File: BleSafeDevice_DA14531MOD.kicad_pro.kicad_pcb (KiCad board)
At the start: 2 copper layers, 43.5 x 33.5 mm, 21 parts, among them J1 Conn_01x04, J2 EXT_PWR, SW1 1825910-6, U4 DA14531MOD-00F01002

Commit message: Sync PCB with schematic cleanup
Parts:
- removed D2: BAT54, myparts:SOT95P240X120-3N
- removed S1: MSK12C02, Button_Switch_SMD:SW_SPDT_PCM12
- C1: value 47uF 6.3V -> 100uF 6.3V
- D1: value LED_ARGB -> LRTBR48G-P9Q7-1; footprint LED_SMD:LED_RGB_Wuerth-PLCC4_3.2x2.8mm_150141M173100 -> SafeGuardPing_Local:LED_RGB_amsOSRAM_LRTBR48G
- J2: value EXT_PWR -> CURRENT_MEAS_PADS
- JP1: value JP_EXT_TO_VCC -> CURRENT_MEAS_JUMPER
- SW1: value 1825910-6 -> PTS526SK15SMTR2 LFS; footprint 1825910-6:SW4_1825910-B_TEC -> SafeGuardPing_Local:SW_Push_1P1T_NO_CK_PTS526SK15SMTR2_LFS
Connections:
- J2 pad 1: Net-(J2-Pin_1) -> VBAT
- JP1 pad 1: Net-(J2-Pin_1) -> VBAT

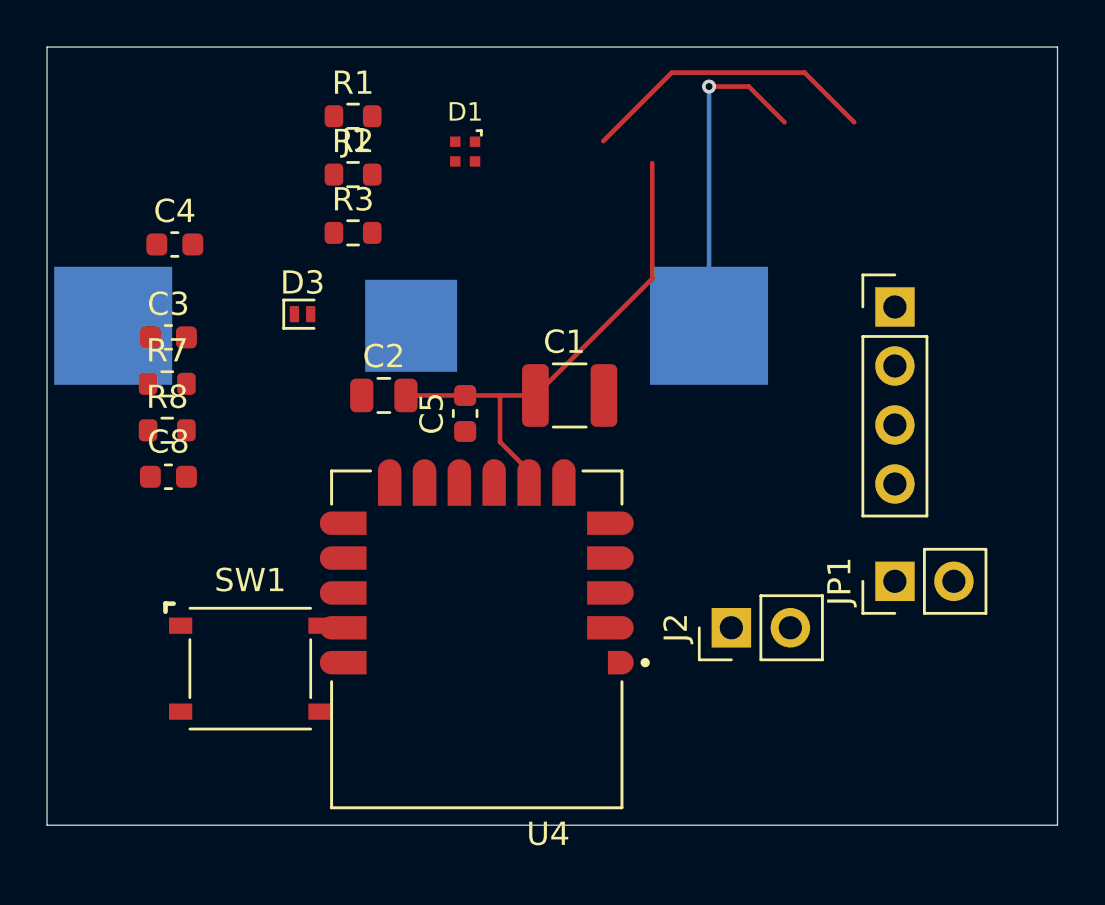
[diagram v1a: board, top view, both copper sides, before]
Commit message: Clean PCB placement after schematic sync
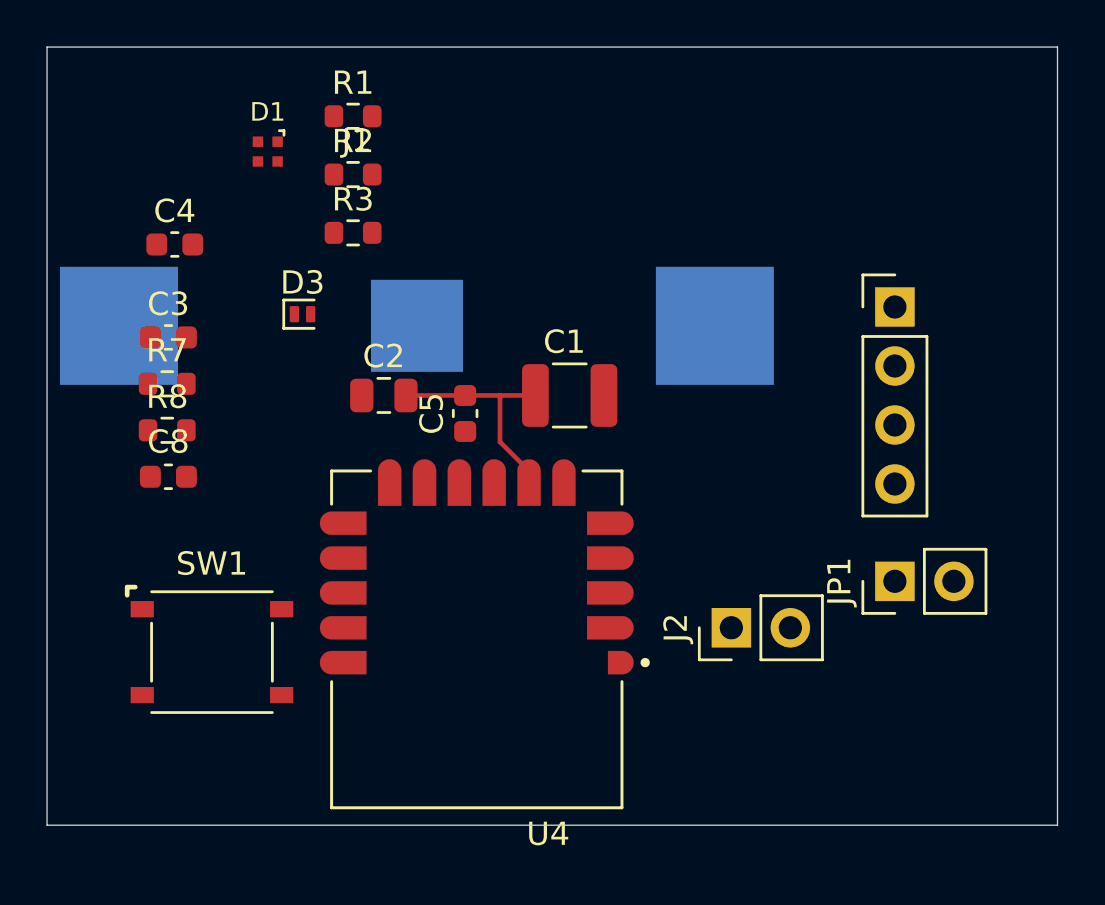
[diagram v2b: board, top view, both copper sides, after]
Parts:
- moved D1 8.50 mm to (108.5, 101.0)
- moved SW1 1.80 mm to (106.1, 122.5)
- moved BT1 0.25 mm to (114.9, 108.5)
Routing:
- net VBAT: track 14.2 -> 0.00 mm, vias 1 -> 0
- net Net-(D2-Pad1): track 12.9 -> 0.00 mm
- net VCC: track 21.9 -> 9.84 mm
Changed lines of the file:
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@@
 	(net 6 "Net-(D1-GK)")
 	(net 7 "Net-(D1-RK)")
-	(net 8 "Net-(D2-Pad1)")
-	(net 9 "Net-(D3-K)")
-	(net 10 "/SWCLK")
-	(net 11 "/SWDIO")
-	(net 12 "LED_R")
-	(net 13 "LED_G")
-	(net 14 "LED_B")
-	(net 15 "unconnected-(U4-P0_0{slash}RST-PadJ12)")
-	(net 16 "unconnected-(U4-P0_5-PadJ14)")
-	(net 17 "unconnected-(U4-P0_11-PadJ8)")
+	(net 8 "Net-(D3-K)")
+	(net 9 "/SWCLK")
+	(net 10 "/SWDIO")
+	(net 11 "LED_R")
+	(net 12 "LED_G")
+	(net 13 "LED_B")
+	(net 14 "unconnected-(U4-P0_0{slash}RST-PadJ12)")
+	(net 15 "unconnected-(U4-P0_5-PadJ14)")
+	(net 16 "unconnected-(U4-P0_11-PadJ8)")
 	(footprint "Diode_SMD:D_SOD-882"
 		(layer "F.Cu")
@@
 			(layers "F.Cu" "F.Mask")
 			(roundrect_rratio 0.125)
-			(net 9 "Net-(D3-K)")
+			(net 8 "Net-(D3-K)")
 			(pinfunction "K")
 			(pintype "passive")
@@
 	(footprint "SafeGuardPing_Local:LED_RGB_amsOSRAM_LRTBR48G"
 		(layer "F.Cu")
-		(at 117 101)
+		(at 108.5 101)
 		(descr "ams OSRAM LRTB R48G Multi CHIPLED, 1.0 mm x 1.0 mm, common anode; recommended land pattern from OSRAM Data Sheet Version 1.8, 2018-05-14, pages 20-21")
 		(tags "LED RGB common anode LRTB R48G LRTBR48G")
@@
 			(layers "F.Cu" "F.Mask" "F.Paste")
 			(roundrect_rratio 0.25)
-			(net 9 "Net-(D3-K)")
+			(net 8 "Net-(D3-K)")
 			(pintype "passive")
 		)
@@
 			(layers "*.Cu" "*.Mask")
 			(remove_unused_layers no)
-			(net 11 "/SWDIO")
+			(net 10 "/SWDIO")
 			(pinfunction "Pin_2")
 			(pintype "passive")
@@
 			(layers "*.Cu" "*.Mask")
 			(remove_unused_layers no)
-			(net 10 "/SWCLK")
+			(net 9 "/SWCLK")
 			(pinfunction "Pin_3")
 			(pintype "passive")
@@
 	(footprint "SafeGuardPing_Local:SW_Push_1P1T_NO_CK_PTS526SK15SMTR2_LFS"
 		(layer "F.Cu")
-		(at 107.75 123.2606)
+		(at 106.1 122.55)
 		(descr "C&K/Littelfuse PTS526SK15SMTR2 LFS, 1.5 mm height, no ground pin; land pattern from C&K PTS526 Series datasheet, Feb 2022, page B-34")
 		(tags "tactile switch PTS526 PTS526SK15SMTR2 LFS")
@@
 			(size 1 0.7)
 			(layers "F.Cu" "F.Mask" "F.Paste")
-			(net 9 "Net-(D3-K)")
+			(net 8 "Net-(D3-K)")
 		)
 		(pad "2" smd rect
@@
 			(size 1 0.7)
 			(layers "F.Cu" "F.Mask" "F.Paste")
-			(net 9 "Net-(D3-K)")
+			(net 8 "Net-(D3-K)")
 		)
 		(pad "3" smd rect
@@
 			(layers "F.Cu" "F.Mask" "F.Paste")
 			(roundrect_rratio 0.25)
-			(net 14 "LED_B")
+			(net 13 "LED_B")
 			(pintype "passive")
 		)
@@
 			(layers "F.Cu" "F.Mask" "F.Paste")
 			(roundrect_rratio 0.25)
-			(net 12 "LED_R")
+			(net 11 "LED_R")
 			(pintype "passive")
 		)
@@
 			(layers "F.Cu" "F.Mask" "F.Paste")
 			(roundrect_rratio 0.25)
-			(net 13 "LED_G")
+			(net 12 "LED_G")
 			(pintype "passive")
 		)
@@
 			(size 0.1 0.1)
 			(layers "F.Cu")
-			(net 14 "LED_B")
+			(net 13 "LED_B")
 			(pinfunction "P0_6")
 			(pintype "bidirectional")
@@
 			(size 0.1 0.1)
 			(layers "F.Cu")
-			(net 17 "unconnected-(U4-P0_11-PadJ8)")
+			(net 16 "unconnected-(U4-P0_11-PadJ8)")
 			(pinfunction "P0_11")
 			(pintype "bidirectional+no_connect")
@@
 			(size 0.1 0.1)
 			(layers "F.Cu")
-			(net 11 "/SWDIO")
+			(net 10 "/SWDIO")
 			(pinfunction "P0_10/SWDIO")
 			(pintype "bidirectional")
@@
 			(size 0.1 0.1)
 			(layers "F.Cu")
-			(net 10 "/SWCLK")
+			(net 9 "/SWCLK")
 			(pinfunction "P0_2/SWCLK")
 			(pintype "bidirectional")
@@
 			(size 0.1 0.1)
 			(layers "F.Cu")
-			(net 15 "unconnected-(U4-P0_0{slash}RST-PadJ12)")
+			(net 14 "unconnected-(U4-P0_0{slash}RST-PadJ12)")
 			(pinfunction "P0_0/RST")
 			(pintype "bidirectional+no_connect")
@@
 			(size 0.1 0.1)
 			(layers "F.Cu")
-			(net 13 "LED_G")
+			(net 12 "LED_G")
 			(pinfunction "P0_7")
 			(pintype "bidirectional")
@@
 			(size 0.1 0.1)
 			(layers "F.Cu")
-			(net 16 "unconnected-(U4-P0_5-PadJ14)")
+			(net 15 "unconnected-(U4-P0_5-PadJ14)")
 			(pinfunction "P0_5")
 			(pintype "bidirectional+no_connect")
@@
 			(size 0.1 0.1)
 			(layers "F.Cu")
-			(net 12 "LED_R")
+			(net 11 "LED_R")
 			(pinfunction "P0_8")
 			(pintype "bidirectional")
@@
 	(footprint "Keystone-3002:BAT_3002"
 		(layer "B.Cu")
-		(at 114.675 108.5 180)
+		(at 114.925 108.5 180)
 		(property "Reference" "BT1"
 			(at -12.4534 10.709 0)
@@
 	)
 	(segment
-		(start 127.5 98.201)
-		(end 129.211 98.201)
-		(width 0.2)
-		(layer "F.Cu")
-		(net 1)
-	)
-	(segment
-		(start 129.211 98.201)
-		(end 130.75 99.74)
-		(width 0.2)
-		(layer "F.Cu")
-		(net 1)
-	)
-	(via
-		(at 127.5 98.201)
-		(size 0.6)
-		(drill 0.3)
-		(layers "F.Cu" "B.Cu")
-		(net 1)
-	)
-	(segment
-		(start 127.5 98.201)
-		(end 127.5 108.5)
-		(width 0.2)
-		(layer "B.Cu")
-		(net 1)
-	)
-	(segment
 		(start 118.5 113.5)
 		(end 119.75 114.75)
@@
 	)
 	(segment
-		(start 125.055 106.47)
-		(end 120.025 111.5)
-		(width 0.2)
-		(layer "F.Cu")
-		(net 3)
-	)
-	(segment
-		(start 125.055 101.5)
-		(end 125.055 106.47)
-		(width 0.2)
-		(layer "F.Cu")
-		(net 3)
-	)
-	(segment
 		(start 118.5 111.5)
 		(end 120.025 111.5)
@@
 		(net 3)
 	)
-	(segment
-		(start 133.75 99.74)
-		(end 131.611 97.601)
-		(width 0.2)
-		(layer "F.Cu")
-		(net 8)
-	)
-	(segment
-		(start 131.611 97.601)
-		(end 125.894 97.601)
-		(width 0.2)
-		(layer "F.Cu")
-		(net 8)
-	)
-	(segment
-		(start 125.894 97.601)
-		(end 122.945 100.55)
-		(width 0.2)
-		(layer "F.Cu")
-		(net 8)
-	)
 	(zone

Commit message: Replace bulky debug and measurement headers with compact pads
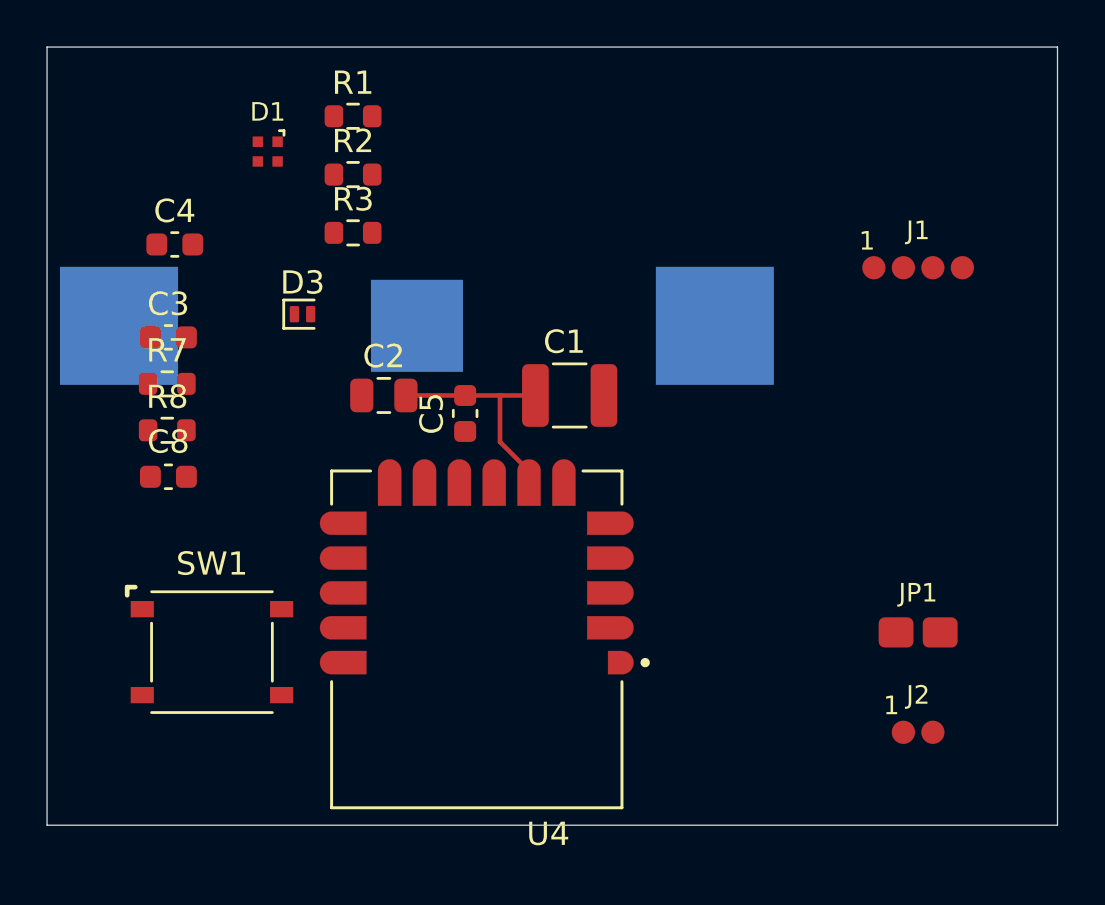
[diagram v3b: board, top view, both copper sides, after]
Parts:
- J1: value Conn_01x04 -> SWD_DEBUG_PADS; footprint Connector_PinHeader_2.54mm:PinHeader_1x04_P2.54mm_Vertical -> SafeGuardPing_Local:TP_SWD_1x04_1.27mm_Compact
- J2: footprint Connector_PinHeader_2.54mm:PinHeader_1x02_P2.54mm_Vertical -> SafeGuardPing_Local:TP_1x02_1.27mm_Compact
- JP1: footprint Connector_PinHeader_2.54mm:PinHeader_1x02_P2.54mm_Vertical -> SafeGuardPing_Local:TP_Current_Jumper_2Pad_Compact
- moved J2 9.21 mm to (136.5, 126.0), turned to 0 degrees
- moved JP1 2.42 mm to (136.5, 121.7), turned to 0 degrees
- moved J1 1.96 mm to (136.5, 106.0)

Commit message: Route coin-cell power and initial ground paths
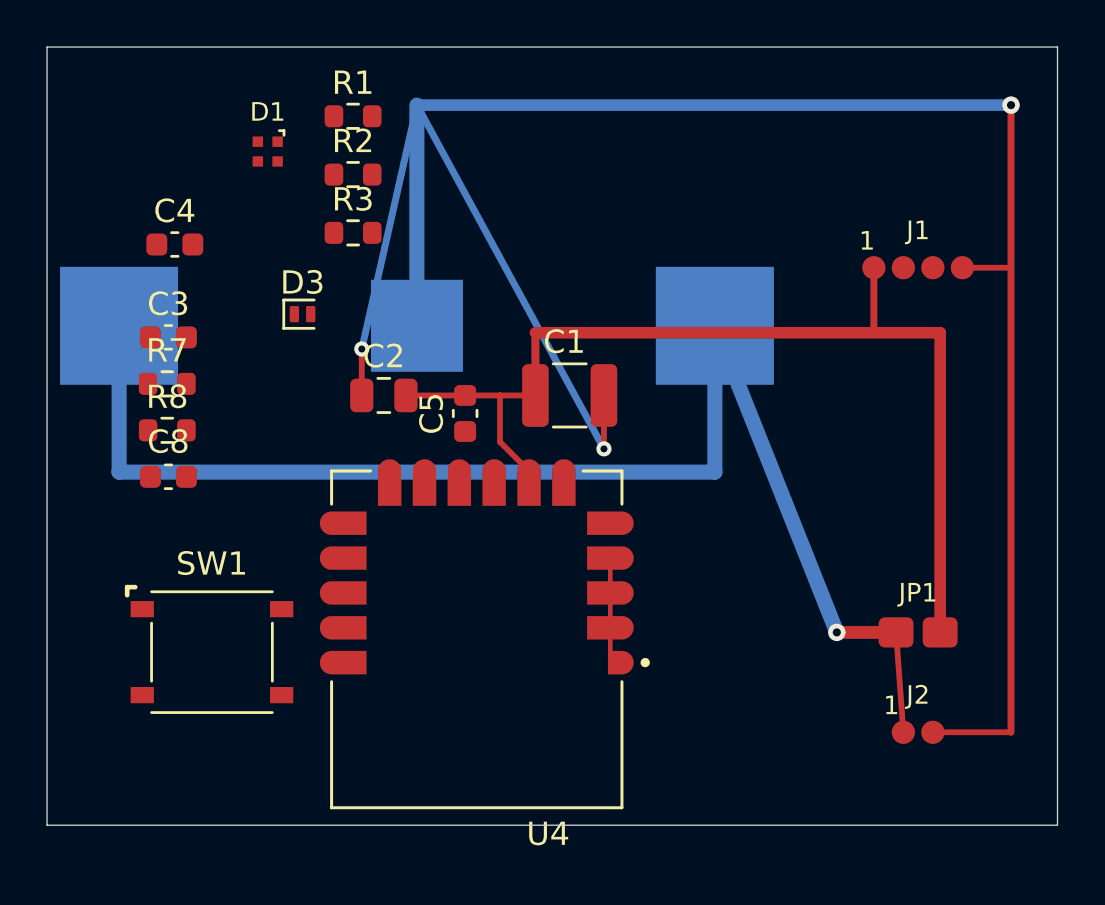
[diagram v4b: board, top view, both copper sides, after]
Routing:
- net GND: track 0.00 -> 103.9 mm, vias 0 -> 3
- net VBAT: track 0.00 -> 59.3 mm, vias 0 -> 1
- net VCC: track 9.84 -> 44.3 mm
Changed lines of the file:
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@@
+	)
+	(segment
+		(start 135.55 121.7)
+		(end 135.865 126)
+		(width 0.25)
+		(layer "F.Cu")
+		(net 1)
+	)
+	(segment
+		(start 133 121.7)
+		(end 135.55 121.7)
+		(width 0.55)
+		(layer "F.Cu")
+		(net 1)
+	)
+	(via
+		(at 133 121.7)
+		(size 0.75)
+		(drill 0.35)
+		(layers "F.Cu" "B.Cu")
+		(net 1)
+	)
+	(segment
+		(start 127.75 108.5)
+		(end 133 121.7)
+		(width 0.65)
+		(layer "B.Cu")
+		(net 1)
+	)
+	(segment
+		(start 102.1 114.8)
+		(end 127.75 114.8)
+		(width 0.65)
+		(layer "B.Cu")
+		(net 1)
+	)
+	(segment
+		(start 102.1 108.5)
+		(end 102.1 114.8)
+		(width 0.65)
+		(layer "B.Cu")
+		(net 1)
+	)
+	(segment
+		(start 127.75 114.8)
+		(end 127.75 108.5)
+		(width 0.65)
+		(layer "B.Cu")
+		(net 1)
+	)
+	(segment
+		(start 140.5 106)
+		(end 138.405 106)
+		(width 0.25)
+		(layer "F.Cu")
+		(net 2)
+	)
+	(segment
+		(start 123.25 121.5)
+		(end 123.25 123)
+		(width 0.2)
+		(layer "F.Cu")
+		(net 2)
+	)
+	(segment
+		(start 140.5 126)
+		(end 137.135 126)
+		(width 0.25)
+		(layer "F.Cu")
+		(net 2)
+	)
+	(segment
+		(start 123.25 118.5)
+		(end 123.25 120)
+		(width 0.2)
+		(layer "F.Cu")
+		(net 2)
+	)
+	(segment
+		(start 123.25 120)
+		(end 123.25 121.5)
+		(width 0.2)
+		(layer "F.Cu")
+		(net 2)
+	)
+	(segment
+		(start 140.5 99)
+		(end 140.5 126)
+		(width 0.3)
+		(layer "F.Cu")
+		(net 2)
+	)
+	(segment
+		(start 112.55 111.5)
+		(end 112.55 109.5)
+		(width 0.25)
+		(layer "F.Cu")
+		(net 2)
+	)
+	(segment
+		(start 122.975 111.5)
+		(end 122.975 113.8)
+		(width 0.25)
+		(layer "F.Cu")
+		(net 2)
+	)
+	(via
+		(at 122.975 113.8)
+		(size 0.65)
+		(drill 0.3)
+		(layers "F.Cu" "B.Cu")
+		(net 2)
+	)
+	(via
+		(at 140.5 99)
+		(size 0.75)
+		(drill 0.35)
+		(layers "F.Cu" "B.Cu")
+		(net 2)
+	)
+	(via
+		(at 112.55 109.5)
+		(size 0.65)
+		(drill 0.3)
+		(layers "F.Cu" "B.Cu")
+		(net 2)
+	)
+	(segment
+		(start 112.55 109.5)
+		(end 114.925 99)
+		(width 0.3)
+		(layer "B.Cu")
+		(net 2)
+	)
+	(segment
+		(start 114.925 99)
+		(end 140.5 99)
+		(width 0.5)
+		(layer "B.Cu")
+		(net 2)
+	)
+	(segment
+		(start 122.975 113.8)
+		(end 114.925 99)
+		(width 0.3)
+		(layer "B.Cu")
+		(net 2)
+	)
+	(segment
+		(start 114.925 108.5)
+		(end 114.925 99)
+		(width 0.65)
+		(layer "B.Cu")
+		(net 2)
 	)
 	(segment
 		(start 118.5 113.5)
 		(end 119.75 114.75)
-		(width 0.2)
+		(width 0.25)
 		(layer "F.Cu")
 		(net 3)
@@
 		(start 118.5 111.5)
 		(end 118.5 113.5)
-		(width 0.2)
+		(width 0.25)
 		(layer "F.Cu")
 		(net 3)
@@
 		(start 119.75 114.75)
 		(end 119.75 115.25)
-		(width 0.2)
+		(width 0.25)
 		(layer "F.Cu")
 		(net 3)
@@
 		(start 118.5 111.5)
 		(end 117 111.5)
-		(width 0.2)
+		(width 0.25)
+		(layer "F.Cu")
+		(net 3)
+	)
+	(segment
+		(start 134.595 106)
+		(end 134.595 108.8)
+		(width 0.3)
+		(layer "F.Cu")
+		(net 3)
+	)
+	(segment
+		(start 137.45 108.8)
+		(end 120.025 108.8)
+		(width 0.5)
 		(layer "F.Cu")
 		(net 3)
@@
 		(start 118.5 111.5)
 		(end 120.025 111.5)
-		(width 0.2)
+		(width 0.25)
 		(layer "F.Cu")
 		(net 3)
@@
 		(start 117 111.5)
 		(end 114.45 111.5)
-		(width 0.2)
-		(layer "F.Cu")
-		(net 3)
+		(width 0.25)
+		(layer "F.Cu")
+		(net 3)
+	)
+	(segment
+		(start 137.45 121.7)
+		(end 137.45 108.8)
+		(width 0.5)
+		(layer "F.Cu")
+		(net 3)
+	)
+	(segment
+		(start 120.025 108.8)
+		(end 120.025 110.15)
+		(width 0.35)
+		(layer "F.Cu")
+		(net 3)
